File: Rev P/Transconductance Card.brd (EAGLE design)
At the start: 162.8 x 125.9 mm, 105 parts, among them IC1 74LS00, IC10 LT1991MS, IC11 ADS8319, IC2 74LS00, IC3 74LS07D, IC4 TLC272D, IC5 OP484, IC6 SF_ISC03_DC_DC16-SMD, IC8 ASSR-1530, IC9 ASSR-1530, Q1 2N7000, U1 MCP1700T-3302E/TT, U2 IRF9Z24NPbF, X1 H15MLE

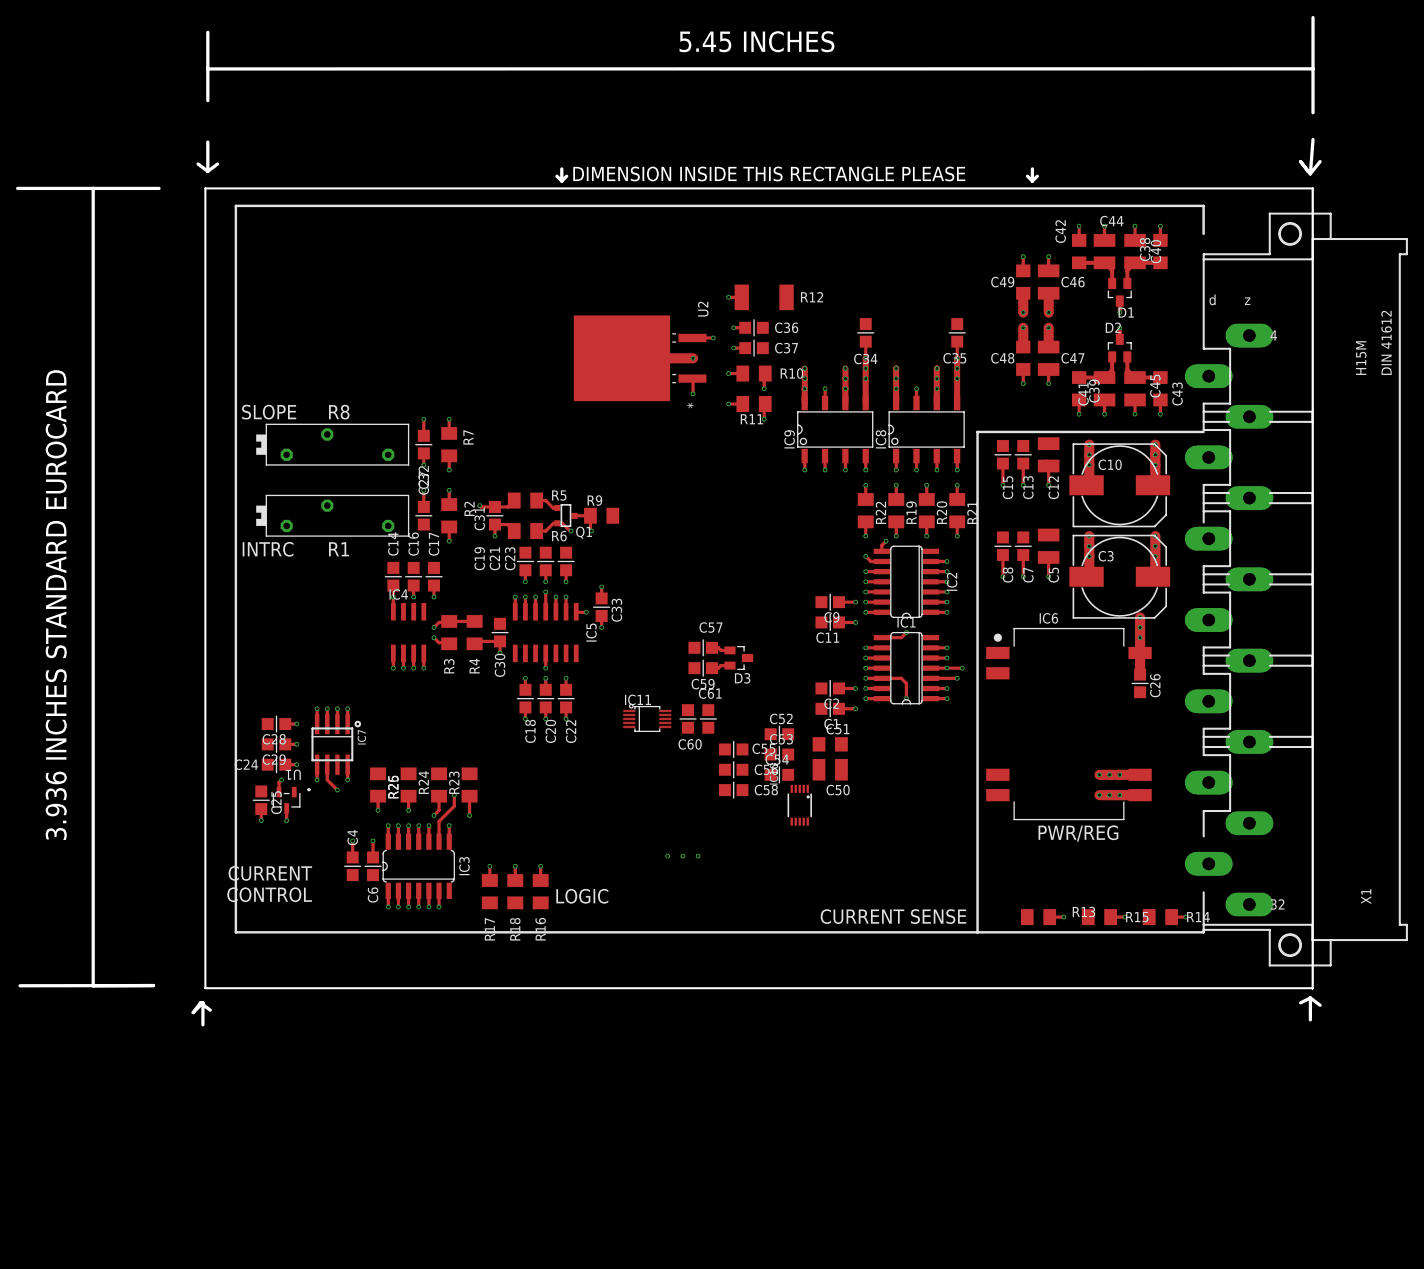
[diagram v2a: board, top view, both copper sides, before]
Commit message: Routing Complete
Still need to heat sink main fet and clean silk screen
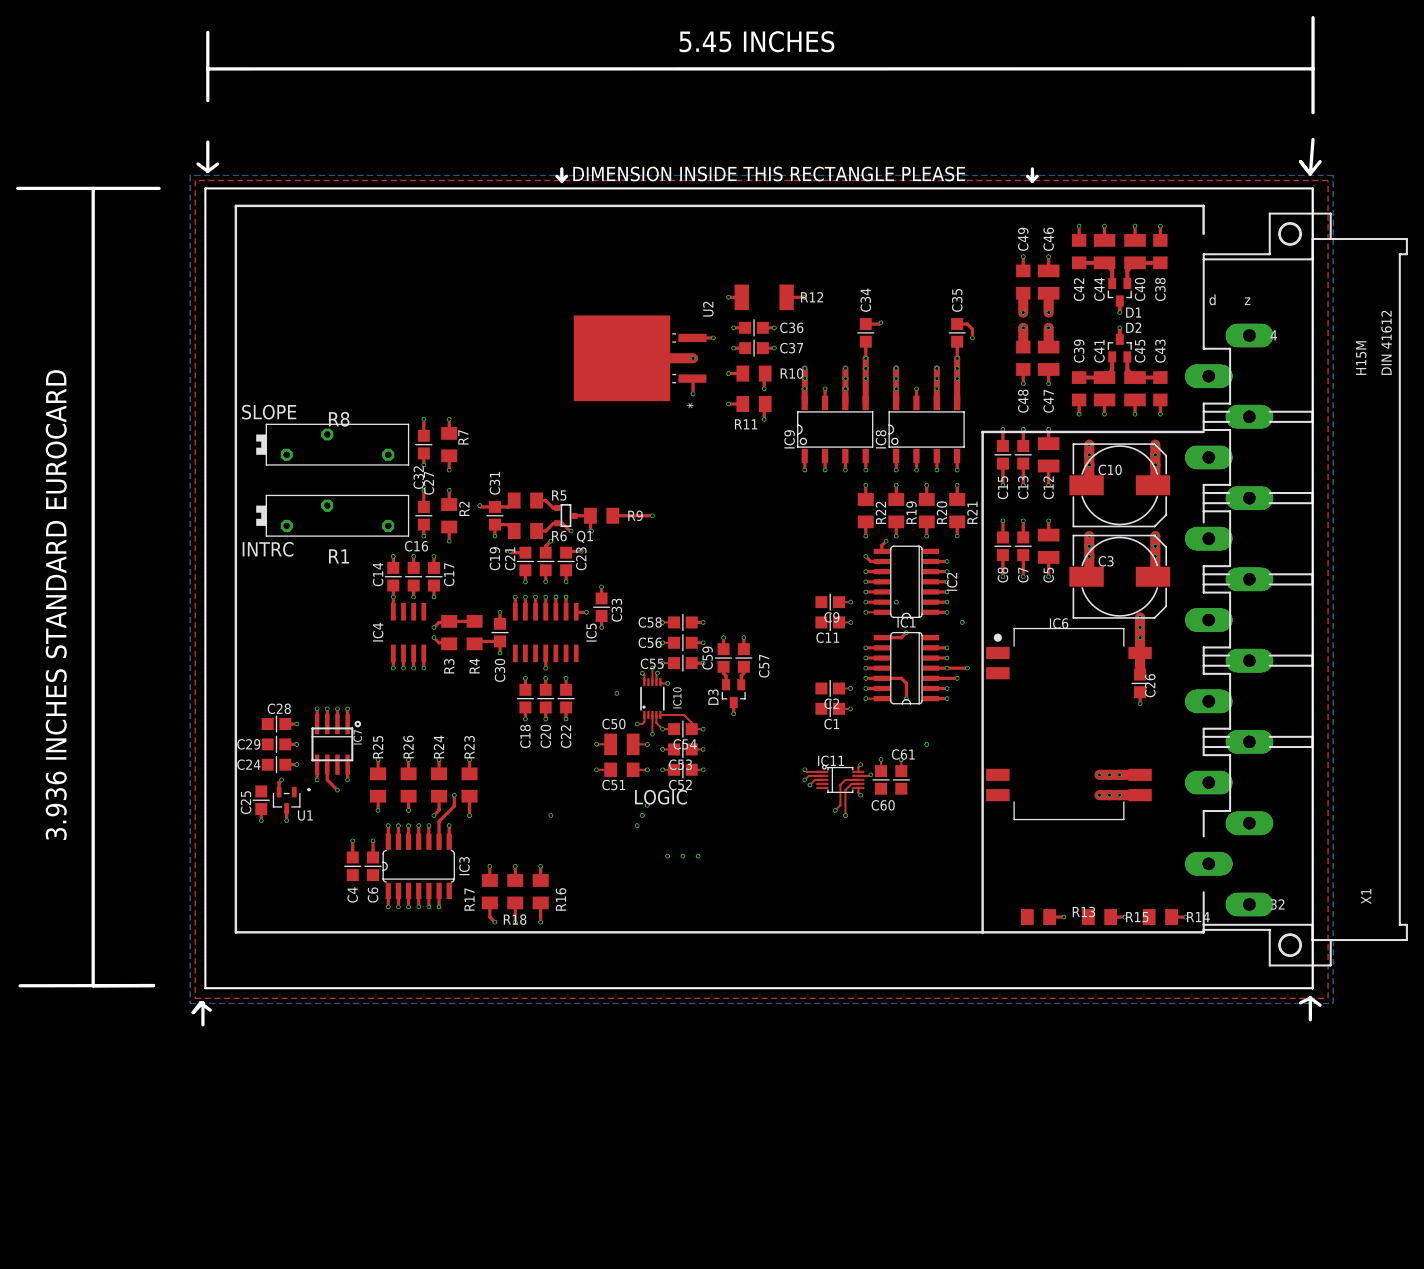
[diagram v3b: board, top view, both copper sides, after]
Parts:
- moved C50 26.2 mm to (52.1, 30.5), turned to 180 degrees
- moved C51 26.2 mm to (52.1, 27.3), turned to 180 degrees
- moved C60 25.3 mm to (84.5, 26.0)
- moved C61 25.3 mm to (87.0, 26.0)
- moved IC11 25.3 mm to (79.4, 26.0)
- moved IC10 22.7 mm to (55.9, 36.2), turned to 0 degrees
- moved C58 21.9 mm to (59.7, 45.7), turned to 0 degrees
- moved C56 17.1 mm to (59.7, 43.2), turned to 0 degrees
- moved C54 13.4 mm to (59.7, 32.4), turned to 180 degrees
- moved C52 12.9 mm to (59.7, 27.3), turned to 180 degrees
- moved C55 12.5 mm to (59.7, 40.6), turned to 0 degrees
- moved C53 12.1 mm to (59.7, 29.8), turned to 180 degrees
- moved C57 5.24 mm to (67.3, 41.3), turned to 90 degrees
- moved D3 4.49 mm to (66.0, 36.8), turned to 180 degrees
- moved C59 2.84 mm to (64.8, 41.3), turned to 90 degrees
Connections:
- removed net +3V3: R26.1
- removed net GND: C34.2, C35.2, C36.2, C37.2, C38.2, C39.2, C40.2, C41.2, C42.2, C43.2, C44.2, C45.2, C46.2, C47.2, C48.2, C49.2, C50.2, C51.2, C52.1, C53.1, C54.1, C55.2, C56.2, C57.2, C58.2, C59.2, C60.2, C61.2, IC10.5, IC11.4, IC11.5, IC8.7, IC9.7, X1.D14, X1.Z12
- removed net VDD: C1.1, C11.1, C2.1, C9.1, IC1.14, IC2.14
- net +3.3V: now also R26.1
- net +5V: now also C1.1, C11.1, C2.1, C9.1, IC1.14, IC2.14
- net AGND: now also C34.2, C35.2, C36.2, C37.2, C38.2, C39.2, C40.2, C41.2, C42.2, C43.2, C44.2, C45.2, C46.2, C47.2, C48.2, C49.2, C50.2, C51.2, C52.1, C53.1, C54.1, C55.2, C56.2, C57.2, C58.2, C59.2, IC10.5, IC8.7, IC9.7, X1.Z12
- net DGND: now also C60.2, C61.2, IC11.4, IC11.5, X1.D14
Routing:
- net +5V: track 41.6 -> 393.8 mm, vias 15 -> 33
- net +20V: track 49.3 -> 192.8 mm, vias 6 -> 13
- net -5V: track 19.3 -> 134.3 mm, vias 7 -> 12
- net +24V: track 77.7 -> 191.7 mm, vias 13 -> 17
- net AGND: track 20.0 -> 97.8 mm, vias 12 -> 54
- net LSENSE: track 26.2 -> 97.6 mm, vias 5 -> 7
- net N$8: track 7.48 -> 75.9 mm, vias 2 -> 4
- net N$4: track 6.21 -> 63.6 mm, vias 2 -> 4
- net N$3: track 7.48 -> 61.0 mm, vias 2 -> 5
- net N$1: track 0.00 -> 33.7 mm, vias 0 -> 3
- net GND: track 24.9 -> 0.00 mm, vias 14 -> 0
- net N$7: track 5.28 -> 25.6 mm, vias 2 -> 4
- net VDD: track 19.5 -> 0.00 mm, vias 6 -> 0
- net +3.3V: track 35.8 -> 45.4 mm, vias 6 -> 7
- net N$15: track 51.5 -> 50.4 mm
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- added copper zone on layer 16, net AGND
- added copper zone on layer 1, net DGND
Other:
- board text removed: "CURRENT CONTROL"
- board text removed: "CURRENT SENSE"
- board text removed: "PWR/REG"

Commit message: Board Routing Finished
Need to clean up silkscreen still
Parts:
- U2: device UL_IRF9Z24:D2PAK -> MeRCIS Lab Parts:UL_IRF9Z24_D2PAK
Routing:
- net H-BDG: vias 7 -> 79
- added copper zone on layer 1, net GND
- added copper zone on layer 16, net GND
- added copper zone on layer 1, net H-BDG
- added copper zone on layer 16, net H-BDG
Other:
- board size 162.8 x 125.9 mm -> 138.4 x 100 mm
